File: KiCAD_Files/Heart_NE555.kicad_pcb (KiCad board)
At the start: 2 copper layers, 50 x 40 mm, 43 parts, among them SW1 SW_DIP_x01, U1 NE555, U2 4017, U3 4017, U4 4017

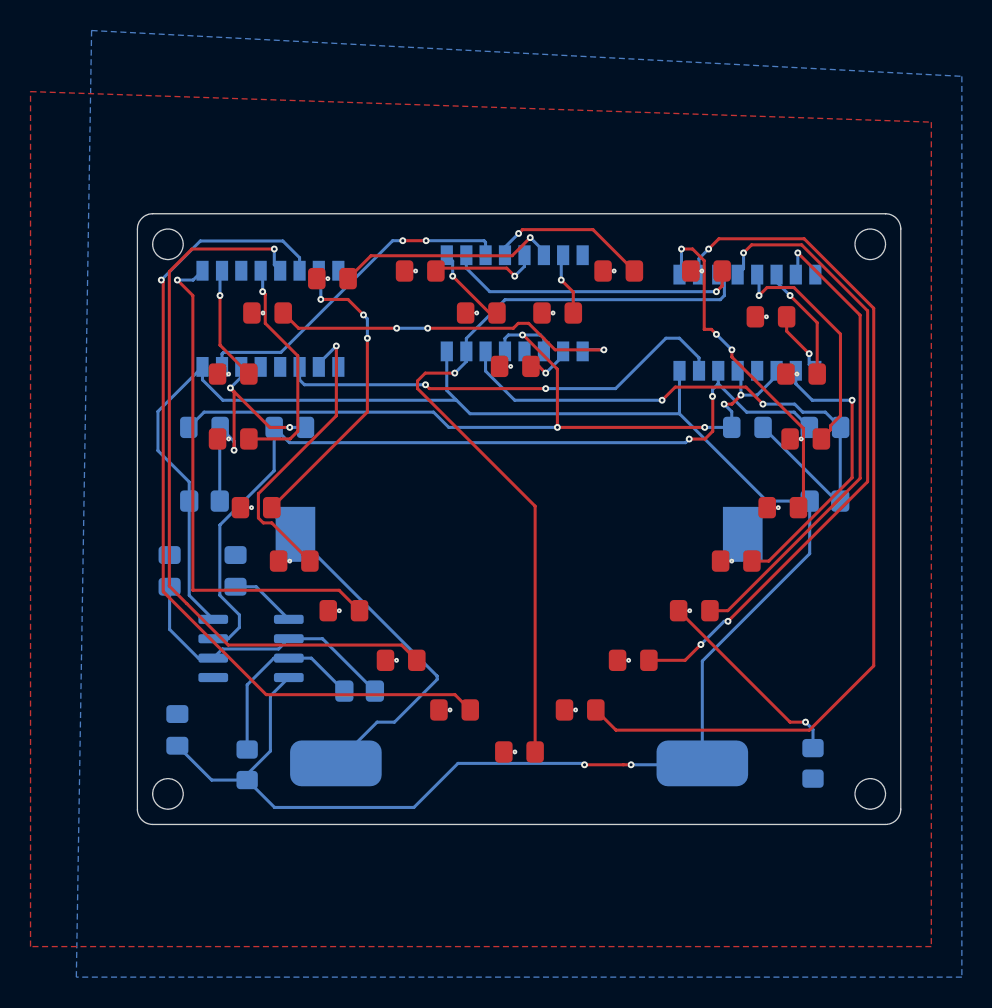
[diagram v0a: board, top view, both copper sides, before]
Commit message: fixed an naming error
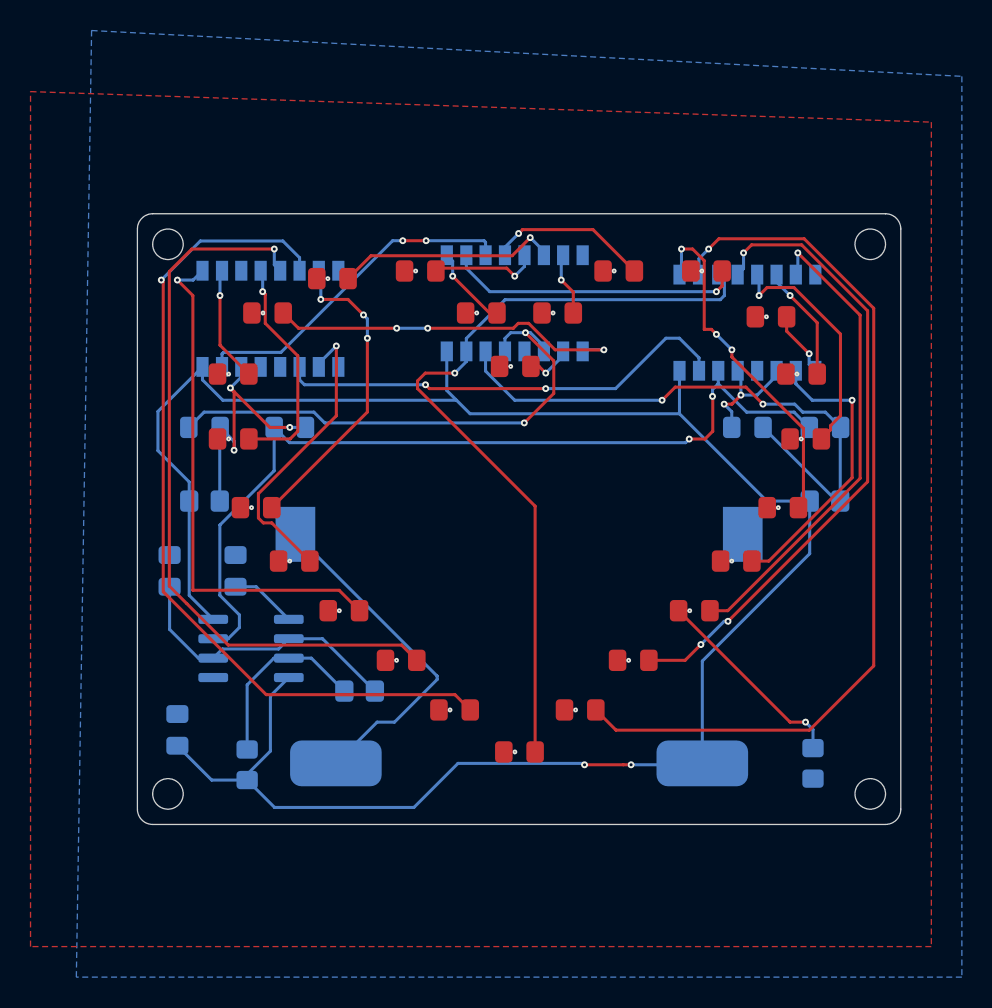
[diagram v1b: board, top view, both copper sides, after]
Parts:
- U1: value NE555 -> NE555D
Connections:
- net /b renamed Net-(D2-Pad1)
- net /out renamed Net-(D3-Pad2)
- D1 pad 1: /a -> Net-(D1-Pad1)
- D3 pad 1: /a -> Net-(D3-Pad1)
- U2 pad 11: /a -> Net-(D3-Pad1)
- U2 pad 13: /a -> Net-(D3-Pad1)
- U3 pad 11: /a -> Net-(D1-Pad1)
- U3 pad 13: /a -> Net-(D1-Pad1)
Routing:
- net /a: track 55.8 -> 0.00 mm, vias 5 -> 0
- net Net-(D1-Pad1): track 0.00 -> 34.4 mm, vias 0 -> 2
- net Net-(D3-Pad1): track 0.00 -> 7.94 mm, vias 0 -> 2

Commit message: changed footprints of diodes, fixed last-led-bug
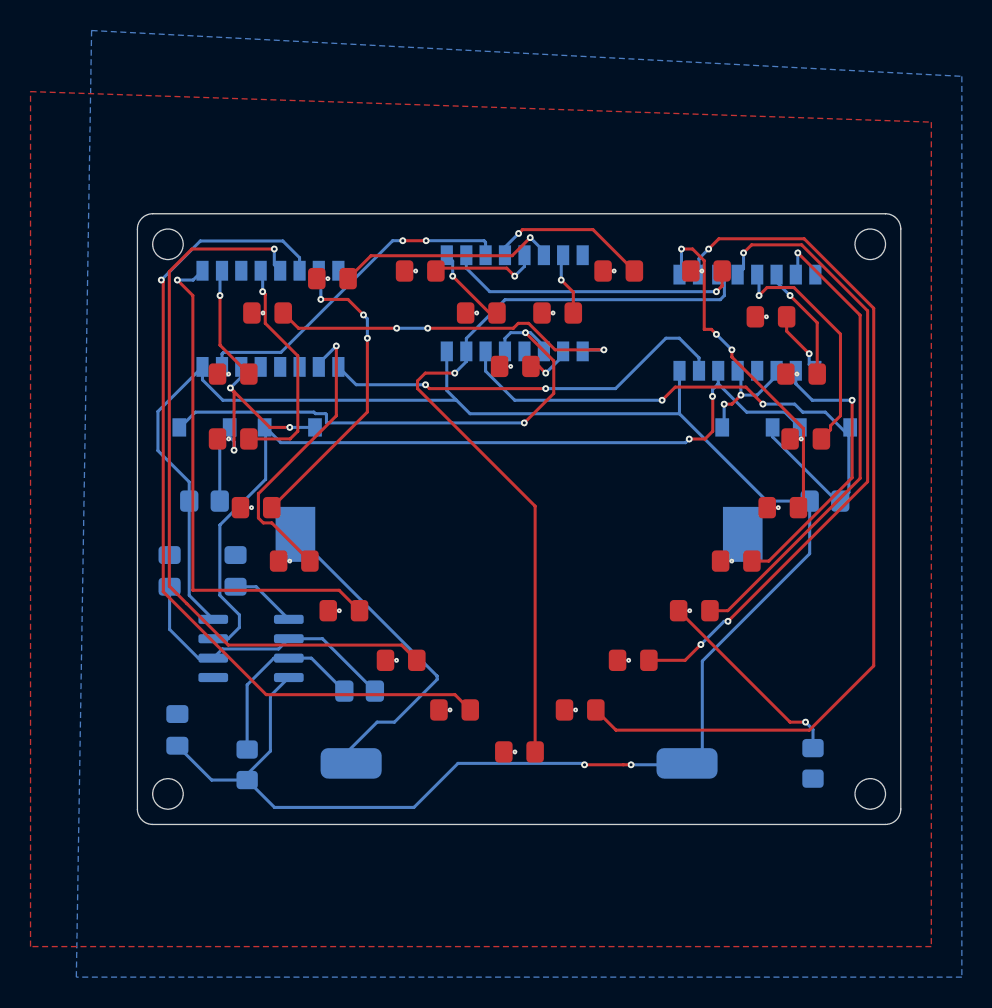
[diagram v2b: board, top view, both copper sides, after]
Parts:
- C1: value C -> 1µ
- C2, C3: value C -> 100n
- D1, D2, D3, D4: value D -> 1N4007; footprint Diode_SMD:D_0805_2012Metric_Pad1.15x1.40mm_HandSolder -> Diode_SMD:D_SOD-123
- R1: value R -> 47k
- R2: value R -> 1k
- R3, R4: value R -> 100k
- R5: value R -> 47R
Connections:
- U4 pad 11: Net-(U2-Pad15) -> Net-(U4-Pad11)
- U4 pad 9: Net-(U4-Pad9) -> Net-(U2-Pad15)
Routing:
- net Net-(U2-Pad15): track 30.0 -> 27.0 mm
- net Net-(D1-Pad1): track 34.4 -> 35.3 mm
- net Net-(D1-Pad2): track 18.6 -> 19.3 mm

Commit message: increased version number, minor changes
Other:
- board text added: "v1.1"
- board text removed: "v1.0"
